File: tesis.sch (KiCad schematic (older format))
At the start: 1 part

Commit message: Agrego v1.0 de SmartSaffron
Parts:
- J1: renamed from J?; value Screw_Terminal_01x02 -> VAC_IN; footprint (none) -> 00_lib_fp:TerminalBlock_Phoenix_MKDS-1,5-2-5.08_1x02_P5.08mm_Horizontal; symbol Connector:Screw_Terminal_01x02 -> 00_lib_sch:Screw_Terminal_01x02
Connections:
- net labels added: [24VAC_main], [AGND_main]
- net labels removed: 24VAC_IN, AGND_IN
- wire segments 6 -> 35
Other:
- note added: "MAIN"
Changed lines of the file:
@@
 $Descr A4 11693 8268
 encoding utf-8
-Sheet 1 5
+Sheet 1 9
 Title ""
-Date ""
-Rev ""
+Date "2021-10-03"
+Rev "v1.0"
 Comp ""
 Comment1 ""
@@
 $EndDescr
 $Sheet
-S 4700 1450 2000 4200
+S 3550 3800 850  950
+U 61438B2D
+F0 "inputs" 50
+F1 "inputs.sch" 50
+F2 "[SCL_inputs]" O R 4400 4650 50
+F3 "[SDA_inputs]" B R 4400 4550 50
+$EndSheet
+Wire Wire Line
+	4900 4550 4400 4550
+Wire Wire Line
+	4400 4650 4900 4650
+Wire Wire Line
+	7450 3100 6900 3100
+Wire Wire Line
+	6900 3200 7450 3200
+Wire Wire Line
+	7450 2350 6900 2350
+Wire Wire Line
+	6900 2450 7450 2450
+Wire Wire Line
+	6900 3550 7450 3550
+Wire Wire Line
+	6900 3450 7450 3450
+Wire Wire Line
+	6900 5100 7450 5100
+Wire Wire Line
+	7450 5200 6900 5200
+Wire Wire Line
+	6900 5300 7450 5300
+Wire Wire Line
+	6900 5500 7450 5500
+$Sheet
+S 7450 1600 850  950
+U 61434A7C
+F0 "Outputs" 50
+F1 "Outputs.sch" 50
+F2 "[SCL_outputs]" I L 7450 2450 50
+F3 "[SDA_outputs]" B L 7450 2350 50
+F4 "[24VAC_outputs]" I L 7450 1700 50
+F5 "[AGND_outputs]" I L 7450 1800 50
+$EndSheet
+$Sheet
+S 7450 2900 850  750
+U 615DBDE4
+F0 "GPS&RTC" 50
+F1 "GPS&RTC.sch" 50
+F2 "[SDA_rtc]" B L 7450 3450 50
+F3 "[SCL_rtc]" I L 7450 3550 50
+F4 "[TX_gps]" O L 7450 3100 50
+F5 "[RX_gps]" I L 7450 3200 50
+$EndSheet
+$Sheet
+S 4900 1600 2000 4200
 U 61410FC3
 F0 "Core" 50
 F1 "Core.sch" 50
-$EndSheet
-$Sheet
-S 3350 2650 850  950
-U 61438B2D
-F0 "inputs" 50
-F1 "inputs.sch" 50
-F2 "[SCL_inputs]" I R 4200 3500 50
-F3 "[SDA_inputs]" I R 4200 3400 50
-$EndSheet
-$Sheet
-S 3100 1450 1100 700
+F2 "[RED_ALERT_uC]" O R 6900 5100 50
+F3 "[GREEN_ALERT_uC]" O R 6900 5300 50
+F4 "[YELLOW_ALERT_uC]" O R 6900 5200 50
+F5 "[SOUND_ALERT_uC]" O R 6900 5500 50
+F6 "[SDA1_uC]" B L 4900 4550 50
+F7 "[SCL1_uC]" I L 4900 4650 50
+F8 "[SDA2_uC]" B R 6900 2350 50
+F9 "[SCL2_uC]" O R 6900 2450 50
+F10 "[SDA3_uC]" B R 6900 3450 50
+F11 "[SCL3_uC]" O R 6900 3550 50
+F12 "[TX_uC]" O R 6900 3200 50
+F13 "[RX_uC]" I R 6900 3100 50
+F14 "[ADC_uC]" I L 4900 2550 50
+$EndSheet
+Wire Wire Line
+	3100 2300 3200 2300
+Connection ~ 3100 2300
+Wire Wire Line
+	3100 1500 3100 2300
+Wire Wire Line
+	3000 1900 3300 1900
+Connection ~ 3000 1900
+Wire Wire Line
+	3000 1500 3000 1900
+Wire Wire Line
+	1950 1900 3000 1900
+Text Label 3100 1500 1    50   ~ 0
+[AGND_main]
+Wire Wire Line
+	2850 2300 3100 2300
+Text Label 3000 1500 1    50   ~ 0
+[24VAC_main]
+$Sheet
+S 2000 2150 850  500
+U 6196C28E
+F0 "monitor" 50
+F1 "monitor.sch" 50
+F2 "[AGND_in]" I L 2000 2300 50
+F3 "[AGND]" O R 2850 2300 50
+F4 "[current_sen_out]" O R 2850 2550 50
+$EndSheet
+Wire Wire Line
+	3200 2000 3300 2000
+Wire Wire Line
+	3200 2300 3200 2000
+Wire Wire Line
+	1950 2300 1950 2000
+Wire Wire Line
+	2000 2300 1950 2300
+$Comp
+L 00_lib_sch:Screw_Terminal_01x02 J1
+U 1 1 61A1065D
+P 1750 2000
+F 0 "J1" H 1750 1750 50  0000 C CNN
+F 1 "VAC_IN" H 1750 2150 50  0000 C CNN
+F 2 "00_lib_fp:TerminalBlock_Phoenix_MKDS-1,5-2-5.08_1x02_P5.08mm_Horizontal" H 1750 2000 50  0001 C CNN
+F 3 "~" H 1750 2000 50  0001 C CNN
+	1    1750 2000
+	-1   0    0    1
+$EndComp
+Wire Wire Line
+	4450 1750 4400 1750
+$Comp
+L 00_lib_sch:+3.3V #PWR0105
+U 1 1 614E88C6
+P 4450 1750
+F 0 "#PWR0105" H 4450 1600 50  0001 C CNN
+F 1 "+3V3" V 4450 1850 50  0000 L CNN
+F 2 "" H 4450 1750 50  0001 C CNN
+F 3 "" H 4450 1750 50  0001 C CNN
+	1    4450 1750
+	0    1    1    0
+$EndComp
+Wire Wire Line
+	4400 1650 4450 1650
+$Comp
+L 00_lib_sch:+5V #PWR0106
+U 1 1 614E8317
+P 4450 1650
+F 0 "#PWR0106" H 4450 1500 50  0001 C CNN
+F 1 "+5V" V 4450 1750 50  0000 L CNN
+F 2 "" H 4450 1650 50  0001 C CNN
+F 3 "" H 4450 1650 50  0001 C CNN
+	1    4450 1650
+	0    1    1    0
+$EndComp
+Wire Wire Line
+	4500 2250 4400 2250
+Wire Wire Line
+	4500 2300 4500 2250
+$Comp
+L 00_lib_sch:GND #PWR0107
+U 1 1 614E69F7
+P 4500 2300
+F 0 "#PWR0107" H 4500 2050 50  0001 C CNN
+F 1 "GND" H 4505 2127 50  0001 C CNN
+F 2 "" H 4500 2300 50  0001 C CNN
+F 3 "" H 4500 2300 50  0001 C CNN
+	1    4500 2300
+	1    0    0    -1
+$EndComp
+$Sheet
+S 3300 1600 1100 700
 U 61391A6D
 F0 "Power" 50
 F1 "Fuente.sch" 50
-F2 "[24VAC_in]" I L 3100 1750 50
-F3 "[+5VDC]" O R 4200 1500 50
-F4 "[GND_out]" O R 4200 2100 50
-F5 "[+3V3DC]" O R 4200 1600 50
-F6 "[AGND]" I L 3100 1850 50
-$EndSheet
-Text Label 2550 1750 0    50   ~ 0
-24VAC_IN
-Text Label 2550 1850 0    50   ~ 0
-AGND_IN
-$Comp
-L power:GND #PWR?
-U 1 1 614E69F7
-P 4300 2150
-F 0 "#PWR?" H 4300 1900 50  0001 C CNN
-F 1 "GND" H 4305 1977 50  0001 C CNN
-F 2 "" H 4300 2150 50  0001 C CNN
-F 3 "" H 4300 2150 50  0001 C CNN
-	1    4300 2150
-	1    0    0    -1
-$EndComp
-Wire Wire Line
-	4300 2150 4300 2100
-Wire Wire Line
-	4300 2100 4200 2100
-$Comp
-L power:+5V #PWR?
-U 1 1 614E8317
-P 4250 1500
-F 0 "#PWR?" H 4250 1350 50  0001 C CNN
-F 1 "+5V" V 4250 1600 50  0000 L CNN
-F 2 "" H 4250 1500 50  0001 C CNN
-F 3 "" H 4250 1500 50  0001 C CNN
-	1    4250 1500
-	0    1    1    0
-$EndComp
-Wire Wire Line
-	4200 1500 4250 1500
-$Comp
-L power:+3V3 #PWR?
-U 1 1 614E88C6
-P 4250 1600
-F 0 "#PWR?" H 4250 1450 50  0001 C CNN
-F 1 "+3V3" V 4250 1700 50  0000 L CNN
-F 2 "" H 4250 1600 50  0001 C CNN
-F 3 "" H 4250 1600 50  0001 C CNN
-	1    4250 1600
-	0    1    1    0
-$EndComp
-Wire Wire Line
-	4250 1600 4200 1600
-$Comp
-L Connector:Screw_Terminal_01x02 J?
-U 1 1 61A1065D
-P 2100 1850
-F 0 "J?" H 2018 1525 50  0000 C CNN
-F 1 "Screw_Terminal_01x02" H 2018 1616 50  0000 C CNN
-F 2 "" H 2100 1850 50  0001 C CNN
-F 3 "~" H 2100 1850 50  0001 C CNN
-	1    2100 1850
-	-1   0    0    1
-$EndComp
-Wire Wire Line
-	2300 1850 3100 1850
-Wire Wire Line
-	2300 1750 3100 1750
-$Sheet
-S 7250 1450 850  950
-U 61434A7C
-F0 "Outputs" 50
-F1 "Outputs.sch" 50
-F2 "[SCL_outputs]" I L 7250 2300 50
-F3 "[SDA_outputs]" I L 7250 2200 50
-$EndSheet
+F2 "[24VAC_in]" I L 3300 1900 50
+F3 "[+5VDC]" O R 4400 1650 50
+F4 "[GND_out]" O R 4400 2250 50
+F5 "[+3V3DC]" O R 4400 1750 50
+F6 "[AGND]" I L 3300 2000 50
+$EndSheet
+Text Notes 750  1000 0    276  Italic 55
+MAIN
+Wire Notes Line width 39 style solid
+	800  1050 1750 1050
+$Sheet
+S 7450 4350 850  1400
+U 6165BF0A
+F0 "Alerts" 50
+F1 "Alerts.sch" 50
+F2 "[RED_ALERT_in]" I L 7450 5100 50
+F3 "[YELLOW_ALERT_in]" I L 7450 5200 50
+F4 "[GREEN_ALERT_in]" I L 7450 5300 50
+F5 "[SOUND_ALERT_in]" I L 7450 5500 50
+F6 "[24VAC_alerts]" I L 7450 4450 50
+F7 "[AGND_alerts]" I L 7450 4550 50
+$EndSheet
+Text Label 7100 1550 1    50   ~ 0
+[AGND_main]
+Text Label 7200 1550 1    50   ~ 0
+[24VAC_main]
+Wire Wire Line
+	7100 1550 7100 1800
+Wire Wire Line
+	7100 1800 7450 1800
+Wire Wire Line
+	7450 1700 7200 1700
+Wire Wire Line
+	7200 1700 7200 1550
+Text Label 7100 4250 1    50   ~ 0
+[AGND_main]
+Text Label 7200 4250 1    50   ~ 0
+[24VAC_main]
+Wire Wire Line
+	7200 4250 7200 4450
+Wire Wire Line
+	7200 4450 7450 4450
+Wire Wire Line
+	7100 4250 7100 4550
+Wire Wire Line
+	7100 4550 7450 4550
+$Sheet
+S 3900 6150 1200 750
+U 61622184
+F0 "miscleaneous" 50
+F1 "miscleaneous.sch" 50
+$EndSheet
+Wire Wire Line
+	4900 2550 2850 2550
 $EndSCHEMATC

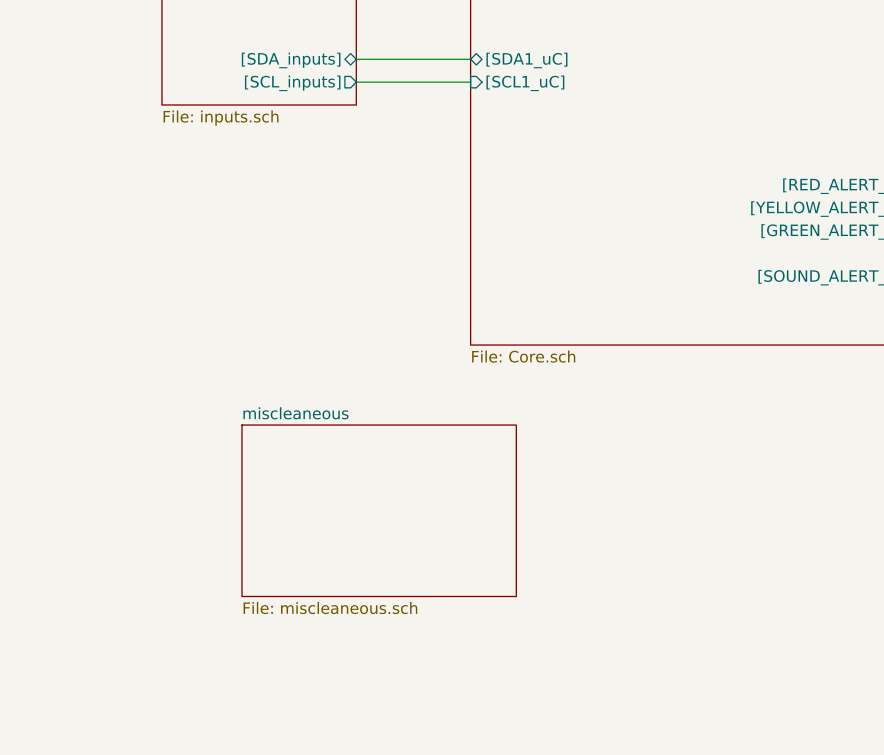
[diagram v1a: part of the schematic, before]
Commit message: Fix por revision grupal
    *Fix de memoria de i2c, mal sda y scl
    *Fix inpunts sda y scl
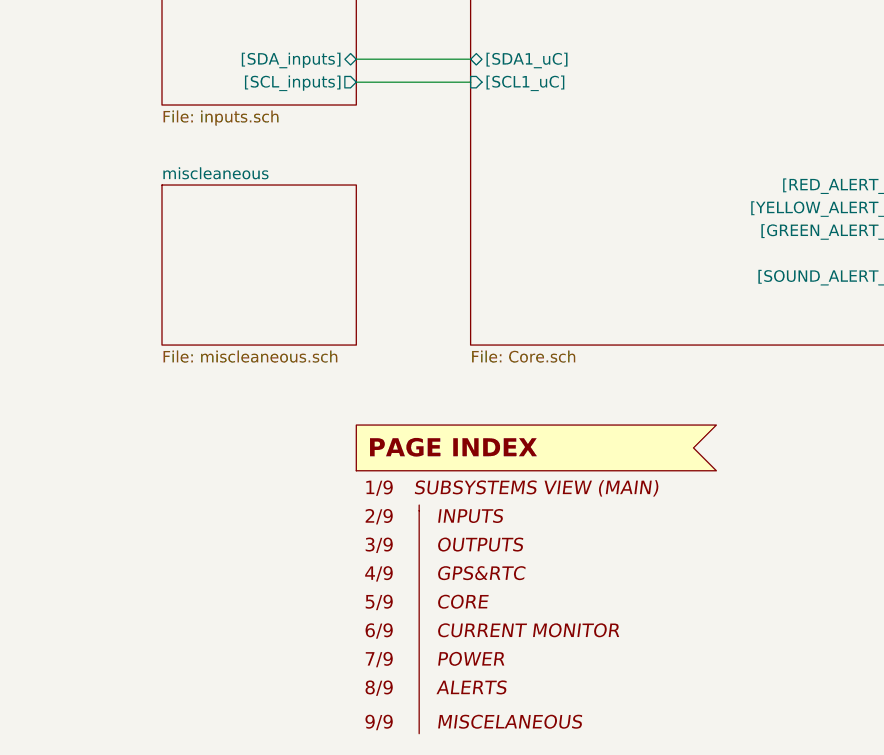
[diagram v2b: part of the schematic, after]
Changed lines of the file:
@@
 	7100 4550 7450 4550
 $Sheet
-S 3900 6150 1200 750
+S 3550 5100 850  700
 U 61622184
 F0 "miscleaneous" 50
@@
 Wire Wire Line
 	4900 2550 2850 2550
+$Comp
+L 00_lib_sch:PageIndex #G?
+U 1 1 616C5ACE
+P 4950 6800
+F 0 "#G?" H 5150 7550 60  0001 C CNN
+F 1 "PageIndex" H 4950 6000 60  0001 C CNN
+F 2 "" H 5025 6725 60  0001 C CNN
+F 3 "" H 5025 6725 60  0001 C CNN
+	1    4950 6800
+	1    0    0    -1
+$EndComp
 $EndSCHEMATC
